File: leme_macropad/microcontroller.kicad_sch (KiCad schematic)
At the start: 23 parts, among them U3 W25Q128JVS, U4 RP2040, Y1 ABM8-272-T3

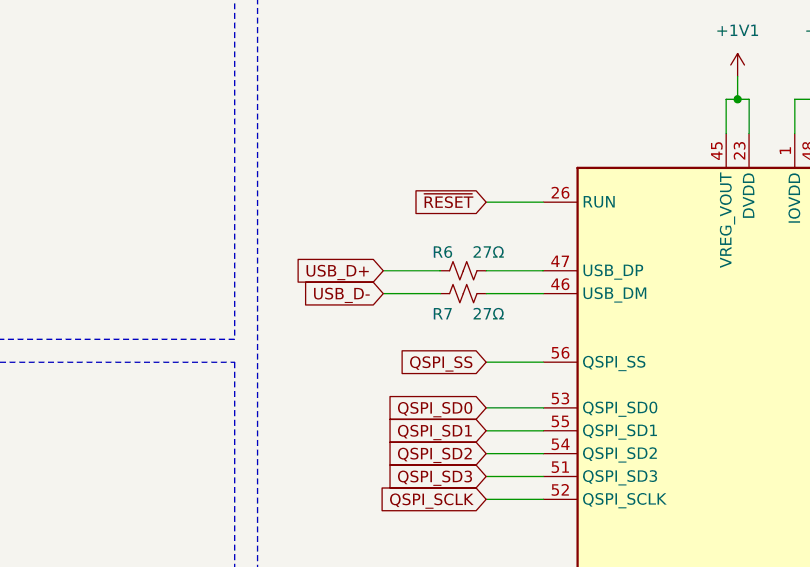
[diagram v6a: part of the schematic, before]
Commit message: Replaces SRV05 with USBLC6 for ESD protection
The USBLC6 is not only built specifically to protect USB data lines, but
is also cheaper than the SRV05.
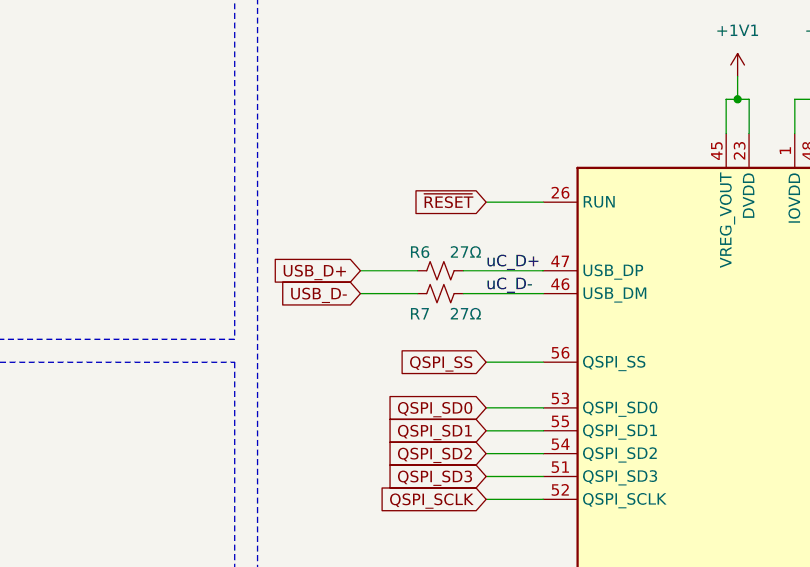
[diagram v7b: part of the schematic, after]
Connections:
- net uC_D+: now reaches R6.2, U4.47 (USB_DP)
- net uC_D-: now reaches R7.2, U4.46 (USB_DM)
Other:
- moved on the sheet: R6, R7
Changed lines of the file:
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@@
 	(wire
 		(pts
-			(xy 199.39 60.96) (xy 205.74 60.96)
-		)
-		(stroke
-			(width 0)
-			(type default)
-		)
-	)
-	(wire
-		(pts
-			(xy 187.96 60.96) (xy 194.31 60.96)
+			(xy 196.85 60.96) (xy 205.74 60.96)
+		)
+		(stroke
+			(width 0)
+			(type default)
+		)
+	)
+	(wire
+		(pts
+			(xy 185.42 60.96) (xy 191.77 60.96)
 		)
 		(stroke
@@
 	(wire
 		(pts
-			(xy 199.39 63.5) (xy 205.74 63.5)
+			(xy 196.85 63.5) (xy 205.74 63.5)
 		)
 		(stroke
@@
 	(wire
 		(pts
-			(xy 187.96 63.5) (xy 194.31 63.5)
+			(xy 185.42 63.5) (xy 191.77 63.5)
 		)
 		(stroke
@@
 		)
 	)
+	(label "uC_D-"
+		(at 199.39 63.5 0)
+		(effects
+			(font
+				(size 1.27 1.27)
+			)
+			(justify left bottom)
+		)
+	)
+	(label "uC_D+"
+		(at 199.39 60.96 0)
+		(effects
+			(font
+				(size 1.27 1.27)
+			)
+			(justify left bottom)
+		)
+	)
 	(global_label "XIN"
 		(shape input)
@@
 	(global_label "USB_D-"
 		(shape input)
-		(at 187.96 63.5 180)
+		(at 185.42 63.5 180)
 		(fields_autoplaced yes)
 		(effects
@@
 		)
 		(property "Intersheetrefs" "${INTERSHEET_REFS}"
-			(at 177.3548 63.5 0)
+			(at 174.8148 63.5 0)
 			(effects
 				(font
@@
 	(global_label "USB_D+"
 		(shape input)
-		(at 187.96 60.96 180)
+		(at 185.42 60.96 180)
 		(fields_autoplaced yes)
 		(effects
@@
 		)
 		(property "Intersheetrefs" "${INTERSHEET_REFS}"
-			(at 177.3548 60.96 0)
+			(at 174.8148 60.96 0)
 			(effects
 				(font
@@
 	(symbol
 		(lib_id "Device:R_Small_US")
-		(at 196.85 60.96 90)
+		(at 194.31 60.96 90)
 		(unit 1)
 		(exclude_from_sim no)
@@
 		(dnp no)
 		(property "Reference" "R6"
-			(at 194.564 58.928 90)
+			(at 192.024 58.928 90)
 			(effects
 				(font
@@
 		)
 		(property "Value" "27Ω"
-			(at 199.644 58.928 90)
+			(at 197.104 58.928 90)
 			(effects
 				(font
@@
 		)
 		(property "Footprint" "Resistor_SMD:R_0402_1005Metric_Pad0.72x0.64mm_HandSolder"
-			(at 196.85 60.96 0)
+			(at 194.31 60.96 0)
 			(effects
 				(font
@@
 		)
 		(property "Datasheet" "~"
-			(at 196.85 60.96 0)
+			(at 194.31 60.96 0)
 			(effects
 				(font
@@
 		)
 		(property "Description" "Resistor, small US symbol"
-			(at 196.85 60.96 0)
+			(at 194.31 60.96 0)
 			(effects
 				(font
@@
 	(symbol
 		(lib_id "Device:R_Small_US")
-		(at 196.85 63.5 90)
+		(at 194.31 63.5 90)
 		(unit 1)
 		(exclude_from_sim no)
@@
 		(dnp no)
 		(property "Reference" "R7"
-			(at 194.564 65.786 90)
+			(at 192.024 65.786 90)
 			(effects
 				(font
@@
 		)
 		(property "Value" "27Ω"
-			(at 199.644 65.786 90)
+			(at 197.104 65.786 90)
 			(effects
 				(font
@@
 		)
 		(property "Footprint" "Resistor_SMD:R_0402_1005Metric_Pad0.72x0.64mm_HandSolder"
-			(at 196.85 63.5 0)
+			(at 194.31 63.5 0)
 			(effects
 				(font
@@
 		)
 		(property "Datasheet" "~"
-			(at 196.85 63.5 0)
+			(at 194.31 63.5 0)
 			(effects
 				(font
@@
 		)
 		(property "Description" "Resistor, small US symbol"
-			(at 196.85 63.5 0)
-			(effects
-				(font
+			(at 194.31 63.5 0)
+			(effects
+				(font

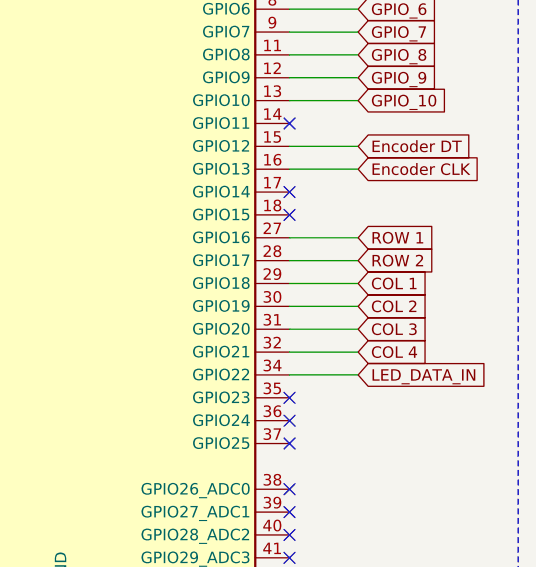
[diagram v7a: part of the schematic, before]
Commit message: Routes keyboard matrix
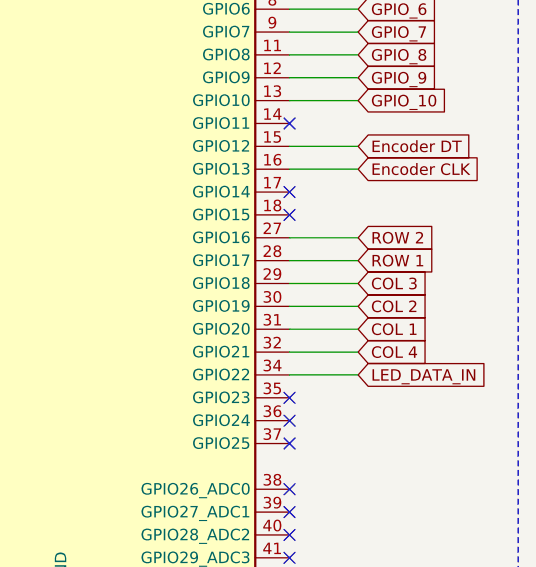
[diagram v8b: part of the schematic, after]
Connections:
- net COL 1: now also U4.31 (GPIO20); no longer U4.29 (GPIO18)
- net COL 3: now also U4.29 (GPIO18); no longer U4.31 (GPIO20)
- net ROW 1: now also U4.28 (GPIO17); no longer U4.27 (GPIO16)
- net ROW 2: now also U4.27 (GPIO16); no longer U4.28 (GPIO17)
